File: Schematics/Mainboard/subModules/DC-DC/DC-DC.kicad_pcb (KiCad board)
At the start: 2 copper layers, 20.1 x 20.1 mm, 9 parts, among them J1 Input, J2 Output, U1 TPS63001

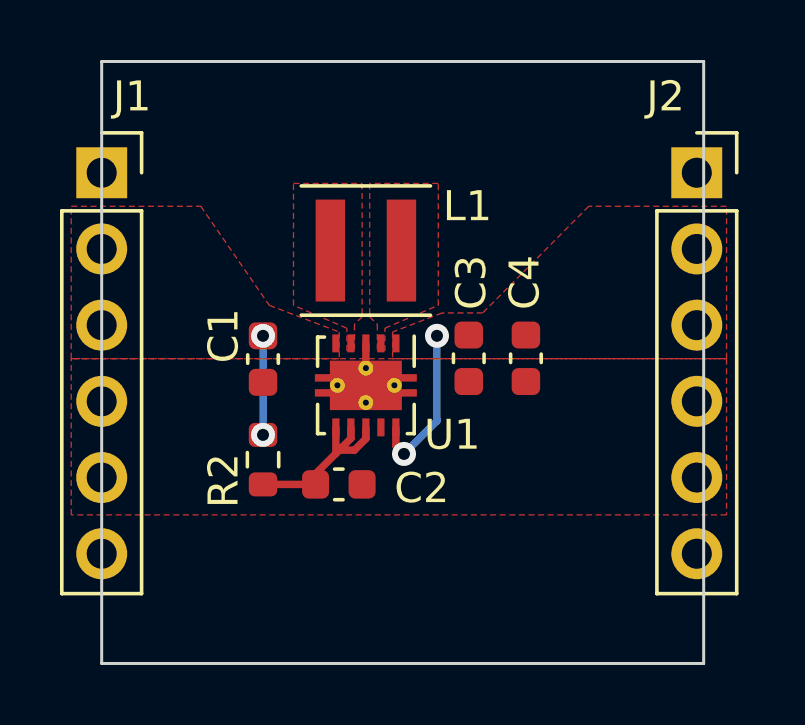
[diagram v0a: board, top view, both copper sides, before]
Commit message: realigned pad
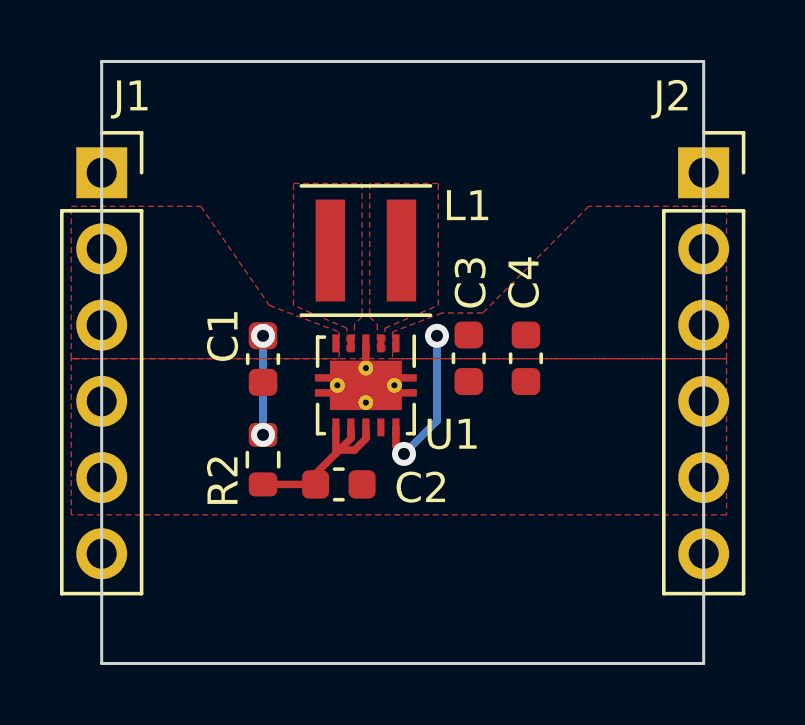
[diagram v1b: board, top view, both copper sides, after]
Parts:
- moved J2 0.23 mm to (109.5, 56.8)
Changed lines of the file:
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@@
   )
   (footprint "Connector_PinSocket_2.54mm:PinSocket_1x06_P2.54mm_Vertical" (layer "F.Cu")
-    (at 109.245 56.794)
+    (at 109.474 56.794)
     (descr "Through hole straight socket strip, 1x06, 2.54mm pitch, single row (from Kicad 4.0.7), script generated")
     (tags "Through hole socket strip THT 1x06 2.54mm single row")
